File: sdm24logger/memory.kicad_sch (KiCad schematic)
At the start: 5 parts, among them J1 Molex_1040310811, U6 ST_EMIF06-MSD02N16, U7 M24128-BRDW6TP

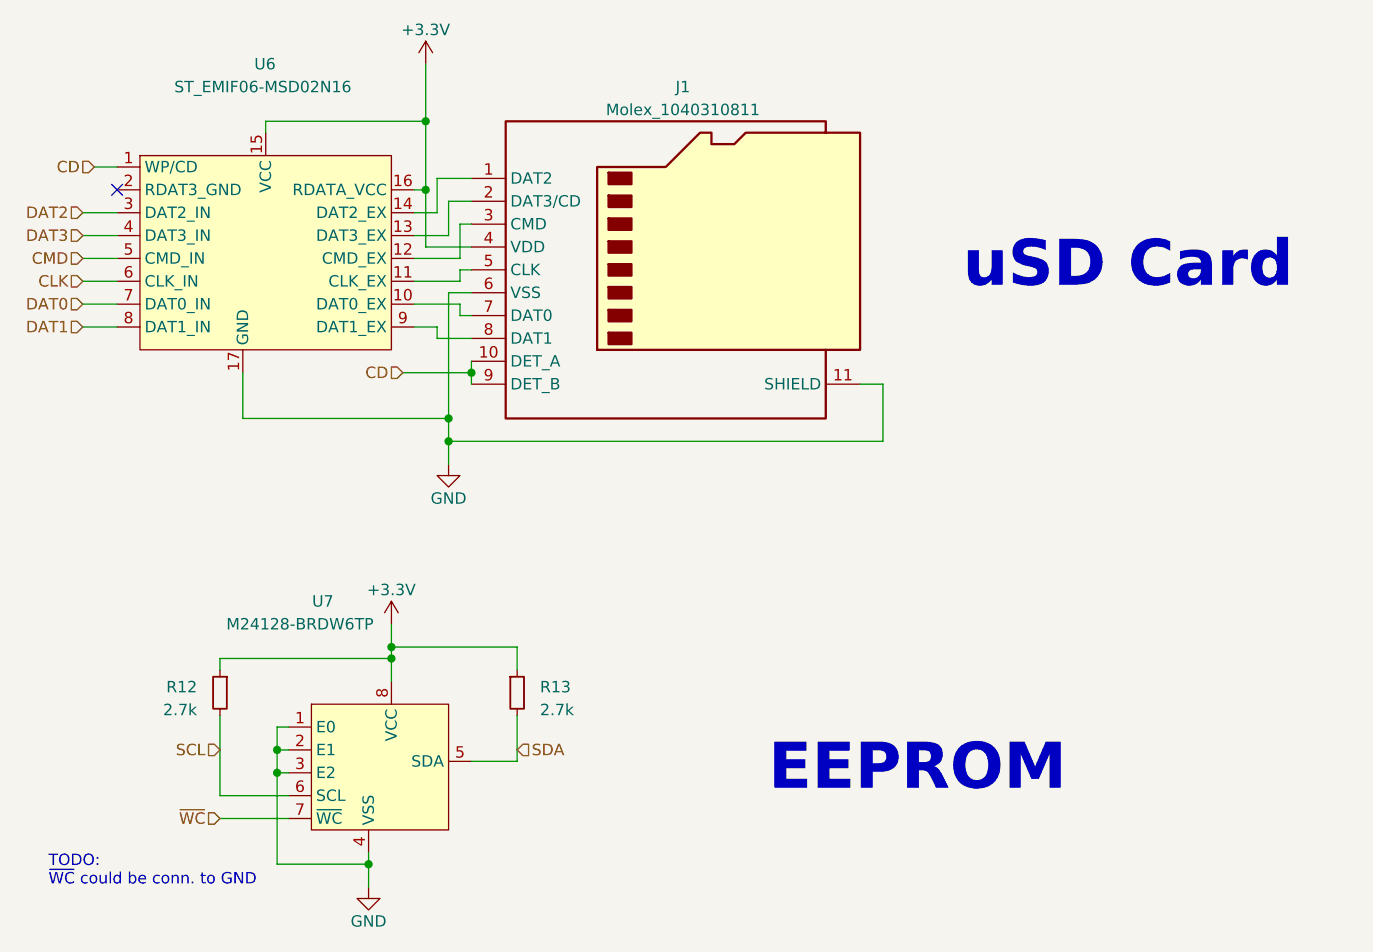
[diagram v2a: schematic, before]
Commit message: add 3d models for data logger
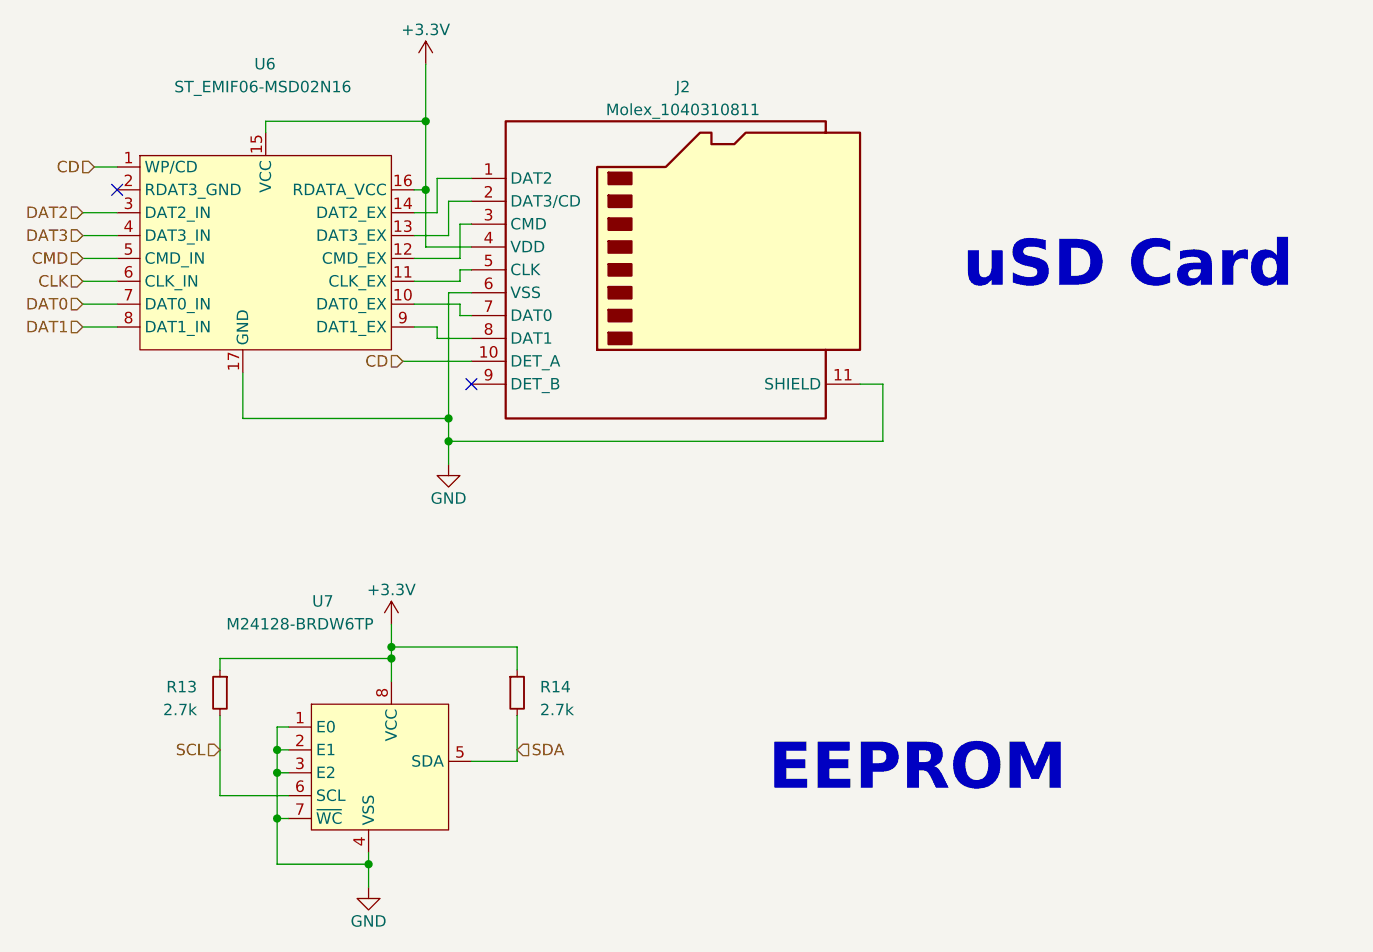
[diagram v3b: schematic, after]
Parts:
- J2: renamed from J1; footprint (none) -> Connector_Card:microSD_HC_Molex_104031-0811
- U7: footprint (none) -> Package_SO:TSSOP-8_4.4x3mm_P0.65mm
- renumbered R12 to R13, R13 to R14
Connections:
- net ~{WC} is gone; now on net GND: U7.7 (~{WC})
- net CD: no longer J2.9 (DET_B)
- no-connect marks 1 -> 2
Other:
- note removed: "TODO: ~{WC} could be conn. to GND"
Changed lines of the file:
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@@
   (title_block
     (title "SDM-24 Data Logger")
-    (date "2023-09-07")
+    (date "2023-10-12")
     (rev "v1")
     (company "Sun Devil Motorsports")
@@
   (junction (at 140.97 86.36) (diameter 0) (color 0 0 0 0)
   )
+  (junction (at 121.92 130.81) (diameter 0) (color 0 0 0 0)
+  )
   (junction (at 121.92 123.19) (diameter 0) (color 0 0 0 0)
   )
-  (junction (at 143.51 81.28) (diameter 0) (color 0 0 0 0)
-  )
+  (no_connect (at 143.51 82.55))
   (no_connect (at 104.14 60.96))
   (wire (pts (xy 189.23 82.55) (xy 189.23 88.9))
@@
     (stroke (width 0) (type default))
   )
-  (wire (pts (xy 115.57 130.81) (xy 123.19 130.81))
-    (stroke (width 0) (type default))
-  )
   (wire (pts (xy 142.24 69.85) (xy 142.24 71.12))
     (stroke (width 0) (type default))
@@
     (stroke (width 0) (type default))
   )
-  (wire (pts (xy 143.51 80.01) (xy 143.51 81.28))
-    (stroke (width 0) (type default))
-  )
   (wire (pts (xy 137.16 76.2) (xy 139.7 76.2))
     (stroke (width 0) (type default))
@@
     (stroke (width 0) (type default))
   )
-  (wire (pts (xy 135.89 81.28) (xy 143.51 81.28))
+  (wire (pts (xy 135.89 80.01) (xy 143.51 80.01))
     (stroke (width 0) (type default))
   )
@@
     (stroke (width 0) (type default))
   )
-  (wire (pts (xy 143.51 81.28) (xy 143.51 82.55))
-    (stroke (width 0) (type default))
-  )
   (wire (pts (xy 115.57 113.03) (xy 134.62 113.03))
     (stroke (width 0) (type default))
@@
     (stroke (width 0) (type default))
   )
+  (wire (pts (xy 121.92 130.81) (xy 121.92 135.89))
+    (stroke (width 0) (type default))
+  )
   (wire (pts (xy 100.33 71.12) (xy 104.14 71.12))
     (stroke (width 0) (type default))
@@
     (stroke (width 0) (type default))
   )
-  (wire (pts (xy 121.92 125.73) (xy 121.92 135.89))
+  (wire (pts (xy 121.92 125.73) (xy 121.92 130.81))
     (stroke (width 0) (type default))
   )
@@
   )
   (wire (pts (xy 189.23 88.9) (xy 140.97 88.9))
+    (stroke (width 0) (type default))
+  )
+  (wire (pts (xy 121.92 130.81) (xy 123.19 130.81))
     (stroke (width 0) (type default))
   )
@@
     (effects (font (size 5.12 5.12) (thickness 1.024) bold) (justify left bottom))
   )
-  (text "TODO: \n~{WC} could be conn. to GND\n" (at 96.52 138.43 0)
-    (effects (font (size 1.27 1.27)) (justify left bottom))
-  )
   (hierarchical_label "CD" (shape input) (at 101.6 58.42 180) (fields_autoplaced)
     (effects (font (size 1.27 1.27)) (justify right))
@@
     (effects (font (size 1.27 1.27)) (justify left))
   )
-  (hierarchical_label "~{WC}" (shape input) (at 115.57 130.81 180) (fields_autoplaced)
-    (effects (font (size 1.27 1.27)) (justify right))
-  )
   (hierarchical_label "DAT0" (shape input) (at 100.33 73.66 180) (fields_autoplaced)
     (effects (font (size 1.27 1.27)) (justify right))
@@
     (effects (font (size 1.27 1.27)) (justify right))
   )
-  (hierarchical_label "CD" (shape input) (at 135.89 81.28 180) (fields_autoplaced)
+  (hierarchical_label "CD" (shape input) (at 135.89 80.01 180) (fields_autoplaced)
     (effects (font (size 1.27 1.27)) (justify right))
   )
   (symbol (lib_id "power:+3.3V") (at 134.62 109.22 0) (unit 1)
     (in_bom yes) (on_board yes) (dnp no) (fields_autoplaced)
-    (property "Reference" "#PWR030" (at 134.62 113.03 0)
+    (property "Reference" "#PWR033" (at 134.62 113.03 0)
       (effects (font (size 1.27 1.27)) hide)
     )
@@
       (project "sdm24logger"
         (path "/89b3ea44-cadd-4bd5-8c60-f45fe49f0b09/755989b5-01b1-4d90-aab7-caeafb9cb82b"
-          (reference "#PWR030") (unit 1)
+          (reference "#PWR033") (unit 1)
         )
       )
@@
   (symbol (lib_id "Device:R_Small") (at 115.57 116.84 0) (mirror y) (unit 1)
     (in_bom yes) (on_board yes) (dnp no)
-    (property "Reference" "R12" (at 113.03 116.205 0)
+    (property "Reference" "R13" (at 113.03 116.205 0)
       (effects (font (size 1.27 1.27)) (justify left))
     )
@@
       (project "sdm24logger"
         (path "/89b3ea44-cadd-4bd5-8c60-f45fe49f0b09/755989b5-01b1-4d90-aab7-caeafb9cb82b"
-          (reference "R12") (unit 1)
+          (reference "R13") (unit 1)
         )
       )
@@
       (effects (font (size 1.27 1.27)))
     )
-    (property "Footprint" "" (at 133.35 110.49 0)
+    (property "Footprint" "Package_SO:TSSOP-8_4.4x3mm_P0.65mm" (at 133.35 110.49 0)
       (effects (font (size 1.27 1.27)) hide)
     )
@@
   (symbol (lib_id "power:GND") (at 140.97 91.44 0) (unit 1)
     (in_bom yes) (on_board yes) (dnp no)
-    (property "Reference" "#PWR032" (at 140.97 97.79 0)
+    (property "Reference" "#PWR035" (at 140.97 97.79 0)
       (effects (font (size 1.27 1.27)) hide)
     )
@@
       (project "sdm24logger"
         (path "/89b3ea44-cadd-4bd5-8c60-f45fe49f0b09/755989b5-01b1-4d90-aab7-caeafb9cb82b"
-          (reference "#PWR032") (unit 1)
+          (reference "#PWR035") (unit 1)
         )
       )
@@
   (symbol (lib_id "power:+3.3V") (at 138.43 46.99 0) (unit 1)
     (in_bom yes) (on_board yes) (dnp no) (fields_autoplaced)
-    (property "Reference" "#PWR031" (at 138.43 50.8 0)
+    (property "Reference" "#PWR034" (at 138.43 50.8 0)
       (effects (font (size 1.27 1.27)) hide)
     )
@@
       (project "sdm24logger"
         (path "/89b3ea44-cadd-4bd5-8c60-f45fe49f0b09/755989b5-01b1-4d90-aab7-caeafb9cb82b"
-          (reference "#PWR031") (unit 1)
+          (reference "#PWR034") (unit 1)
         )
       )
@@
   (symbol (lib_id "Connector:Micro_SD_Card_Det2") (at 166.37 69.85 0) (unit 1)
     (in_bom yes) (on_board yes) (dnp no) (fields_autoplaced)
-    (property "Reference" "J1" (at 167.005 49.53 0)
+    (property "Reference" "J2" (at 167.005 49.53 0)
       (effects (font (size 1.27 1.27)))
     )
@@
       (effects (font (size 1.27 1.27)))
     )
-    (property "Footprint" "" (at 218.44 52.07 0)
+    (property "Footprint" "Connector_Card:microSD_HC_Molex_104031-0811" (at 218.44 52.07 0)
       (effects (font (size 1.27 1.27)) hide)
     )
@@
       (project "sdm24logger"
         (path "/89b3ea44-cadd-4bd5-8c60-f45fe49f0b09/755989b5-01b1-4d90-aab7-caeafb9cb82b"
-          (reference "J1") (unit 1)
+          (reference "J2") (unit 1)
         )
       )
@@
   (symbol (lib_id "Device:R_Small") (at 148.59 116.84 0) (unit 1)
     (in_bom yes) (on_board yes) (dnp no) (fields_autoplaced)
-    (property "Reference" "R13" (at 151.13 116.205 0)
+    (property "Reference" "R14" (at 151.13 116.205 0)
       (effects (font (size 1.27 1.27)) (justify left))
     )
@@
       (project "sdm24logger"
         (path "/89b3ea44-cadd-4bd5-8c60-f45fe49f0b09/755989b5-01b1-4d90-aab7-caeafb9cb82b"
-          (reference "R13") (unit 1)
+          (reference "R14") (unit 1)
         )
       )
@@
   (symbol (lib_id "power:GND") (at 132.08 138.43 0) (unit 1)
     (in_bom yes) (on_board yes) (dnp no)
-    (property "Reference" "#PWR029" (at 132.08 144.78 0)
+    (property "Reference" "#PWR032" (at 132.08 144.78 0)
       (effects (font (size 1.27 1.27)) hide)
     )
@@
       (project "sdm24logger"
         (path "/89b3ea44-cadd-4bd5-8c60-f45fe49f0b09/755989b5-01b1-4d90-aab7-caeafb9cb82b"
-          (reference "#PWR029") (unit 1)
-        )
-      )
+          (reference "#PWR032") (unit 1)
+        )
+      )

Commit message: smps layout, power mux
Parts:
- R13, R14: footprint (none) -> Resistor_SMD:R_0603_1608Metric
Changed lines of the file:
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@@
       (effects (font (size 1.27 1.27)) (justify left))
     )
-    (property "Footprint" "" (at 115.57 116.84 0)
+    (property "Footprint" "Resistor_SMD:R_0603_1608Metric" (at 115.57 116.84 0)
       (effects (font (size 1.27 1.27)) hide)
     )
@@
       (effects (font (size 1.27 1.27)) (justify left))
     )
-    (property "Footprint" "" (at 148.59 116.84 0)
+    (property "Footprint" "Resistor_SMD:R_0603_1608Metric" (at 148.59 116.84 0)
       (effects (font (size 1.27 1.27)) hide)
     )

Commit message: planning for external adc
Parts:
- added C33: 100nF, Capacitor_SMD:C_0402_1005Metric, symbol Device:C_Small
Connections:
- net +3.3V: now also C33.1
- net GND: now also C33.2
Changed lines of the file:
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@@
   (junction (at 140.97 86.36) (diameter 0) (color 0 0 0 0)
+  )
+  (junction (at 134.62 110.49) (diameter 0) (color 0 0 0 0)
   )
   (junction (at 121.92 130.81) (diameter 0) (color 0 0 0 0)
@@
     (stroke (width 0) (type default))
   )
+  (wire (pts (xy 134.62 110.49) (xy 160.02 110.49))
+    (stroke (width 0) (type default))
+  )
   (wire (pts (xy 137.16 66.04) (xy 140.97 66.04))
     (stroke (width 0) (type default))
@@
     (stroke (width 0) (type default))
   )
-  (wire (pts (xy 134.62 109.22) (xy 134.62 111.76))
+  (wire (pts (xy 134.62 110.49) (xy 134.62 111.76))
+    (stroke (width 0) (type default))
+  )
+  (wire (pts (xy 134.62 109.22) (xy 134.62 110.49))
     (stroke (width 0) (type default))
   )
@@
     (stroke (width 0) (type default))
   )
+  (wire (pts (xy 160.02 116.84) (xy 160.02 118.11))
+    (stroke (width 0) (type default))
+  )
   (wire (pts (xy 142.24 74.93) (xy 143.51 74.93))
+    (stroke (width 0) (type default))
+  )
+  (wire (pts (xy 160.02 110.49) (xy 160.02 111.76))
     (stroke (width 0) (type default))
   )
@@
     )
   )
+  (symbol (lib_id "Device:C_Small") (at 160.02 114.3 0) (unit 1)
+    (in_bom yes) (on_board yes) (dnp no) (fields_autoplaced)
+    (property "Reference" "C33" (at 162.56 113.6713 0)
+      (effects (font (size 1.27 1.27)) (justify left))
+    )
+    (property "Value" "100nF" (at 162.56 116.2113 0)
+      (effects (font (size 1.27 1.27)) (justify left))
+    )
+    (property "Footprint" "Capacitor_SMD:C_0402_1005Metric" (at 160.02 114.3 0)
+      (effects (font (size 1.27 1.27)) hide)
+    )
+    (property "Datasheet" "~" (at 160.02 114.3 0)
+      (effects (font (size 1.27 1.27)) hide)
+    )
+    (pin "1")
+    (pin "2")
+    (instances
+      (project "sdm24logger"
+        (path "/89b3ea44-cadd-4bd5-8c60-f45fe49f0b09/755989b5-01b1-4d90-aab7-caeafb9cb82b"
+          (reference "C33") (unit 1)
+        )
+      )
+    )
+  )
   (symbol (lib_id "power:GND") (at 140.97 91.44 0) (unit 1)
     (in_bom yes) (on_board yes) (dnp no)
@@
         )
       )
+    )
+  )
+  (symbol (lib_id "power:GND") (at 160.02 118.11 0) (unit 1)
+    (in_bom yes) (on_board yes) (dnp no)
+    (property "Reference" "#PWR059" (at 160.02 124.46 0)
+      (effects (font (size 1.27 1.27)) hide)
+    )
+    (property "Value" "GND" (at 160.02 121.92 0)
+      (effects (font (size 1.27 1.27)))
+    )
+    (property "Footprint" "" (at 160.02 118.11 0)
+      (effects (font (size 1.27 1.27)) hide)
+    )
+    (property "Datasheet" "" (at 160.02 118.11 0)
+      (effects (font (size 1.27 1.27)) hide)
+    )
+    (pin "1")
+    (instances
+      (project "sdm24logger"
+        (path "/89b3ea44-cadd-4bd5-8c60-f45fe49f0b09/755989b5-01b1-4d90-aab7-caeafb9cb82b"
+          (reference "#PWR059") (unit 1)
+        )
+      )

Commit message: ADC pinouts
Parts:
- removed R13, R14: 2.7k, Resistor_SMD:R_0603_1608Metric, symbol Device:R_Small
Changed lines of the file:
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@@
   (title_block
     (title "SDM-24 Data Logger")
-    (date "2023-10-12")
+    (date "2023-10-22")
     (rev "v1")
     (company "Sun Devil Motorsports")
@@
         (path "/89b3ea44-cadd-4bd5-8c60-f45fe49f0b09/755989b5-01b1-4d90-aab7-caeafb9cb82b"
           (reference "#PWR033") (unit 1)
-        )
-      )
-    )
-  )
-  (symbol (lib_id "Device:R_Small") (at 115.57 116.84 0) (mirror y) (unit 1)
-    (in_bom yes) (on_board yes) (dnp no)
-    (property "Reference" "R13" (at 113.03 116.205 0)
-      (effects (font (size 1.27 1.27)) (justify left))
-    )
-    (property "Value" "2.7k" (at 113.03 118.745 0)
-      (effects (font (size 1.27 1.27)) (justify left))
-    )
-    (property "Footprint" "Resistor_SMD:R_0603_1608Metric" (at 115.57 116.84 0)
-      (effects (font (size 1.27 1.27)) hide)
-    )
-    (property "Datasheet" "~" (at 115.57 116.84 0)
-      (effects (font (size 1.27 1.27)) hide)
-    )
-    (pin "1")
-    (pin "2")
-    (instances
-      (project "sdm24logger"
-        (path "/89b3ea44-cadd-4bd5-8c60-f45fe49f0b09/755989b5-01b1-4d90-aab7-caeafb9cb82b"
-          (reference "R13") (unit 1)
         )
       )
@@
         )
       )
-    )
-  )
-  (symbol (lib_id "Device:R_Small") (at 148.59 116.84 0) (unit 1)
-    (in_bom yes) (on_board yes) (dnp no) (fields_autoplaced)
-    (property "Reference" "R14" (at 151.13 116.205 0)
-      (effects (font (size 1.27 1.27)) (justify left))
-    )
-    (property "Value" "2.7k" (at 151.13 118.745 0)
-      (effects (font (size 1.27 1.27)) (justify left))
-    )
-    (property "Footprint" "Resistor_SMD:R_0603_1608Metric" (at 148.59 116.84 0)
-      (effects (font (size 1.27 1.27)) hide)
-    )
-    (property "Datasheet" "~" (at 148.59 116.84 0)
-      (effects (font (size 1.27 1.27)) hide)
-    )
-    (pin "1")
-    (pin "2")
-    (instances
-      (project "sdm24logger"
-        (path "/89b3ea44-cadd-4bd5-8c60-f45fe49f0b09/755989b5-01b1-4d90-aab7-caeafb9cb82b"
-          (reference "R14") (unit 1)
-        )
-      )

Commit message: uploading changes
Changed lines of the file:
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@@
     (comment 1 "SD card and EEPROM circuitry")
   )
-  (junction (at 134.62 113.03) (diameter 0) (color 0 0 0 0)
-  )
   (junction (at 140.97 88.9) (diameter 0) (color 0 0 0 0)
-  )
-  (junction (at 134.62 111.76) (diameter 0) (color 0 0 0 0)
   )
   (junction (at 132.08 135.89) (diameter 0) (color 0 0 0 0)
@@
     (stroke (width 0) (type default))
   )
-  (wire (pts (xy 134.62 111.76) (xy 134.62 113.03))
+  (wire (pts (xy 134.62 110.49) (xy 134.62 115.57))
     (stroke (width 0) (type default))
   )
@@
     (stroke (width 0) (type default))
   )
-  (wire (pts (xy 115.57 119.38) (xy 115.57 128.27))
-    (stroke (width 0) (type default))
-  )
   (wire (pts (xy 123.19 120.65) (xy 121.92 120.65))
     (stroke (width 0) (type default))
   )
-  (wire (pts (xy 115.57 114.3) (xy 115.57 113.03))
-    (stroke (width 0) (type default))
-  )
   (wire (pts (xy 123.19 125.73) (xy 121.92 125.73))
     (stroke (width 0) (type default))
@@
     (stroke (width 0) (type default))
   )
+  (wire (pts (xy 119.38 128.27) (xy 123.19 128.27))
+    (stroke (width 0) (type default))
+  )
   (wire (pts (xy 137.16 66.04) (xy 140.97 66.04))
     (stroke (width 0) (type default))
@@
     (stroke (width 0) (type default))
   )
-  (wire (pts (xy 134.62 113.03) (xy 134.62 115.57))
-    (stroke (width 0) (type default))
-  )
   (wire (pts (xy 138.43 60.96) (xy 138.43 53.34))
     (stroke (width 0) (type default))
@@
     (stroke (width 0) (type default))
   )
-  (wire (pts (xy 134.62 110.49) (xy 134.62 111.76))
-    (stroke (width 0) (type default))
-  )
   (wire (pts (xy 134.62 109.22) (xy 134.62 110.49))
     (stroke (width 0) (type default))
   )
-  (wire (pts (xy 148.59 124.46) (xy 143.51 124.46))
-    (stroke (width 0) (type default))
-  )
   (wire (pts (xy 100.33 68.58) (xy 104.14 68.58))
     (stroke (width 0) (type default))
@@
     (stroke (width 0) (type default))
   )
-  (wire (pts (xy 148.59 114.3) (xy 148.59 111.76))
-    (stroke (width 0) (type default))
-  )
   (wire (pts (xy 142.24 73.66) (xy 142.24 74.93))
     (stroke (width 0) (type default))
@@
     (stroke (width 0) (type default))
   )
-  (wire (pts (xy 148.59 119.38) (xy 148.59 124.46))
+  (wire (pts (xy 143.51 124.46) (xy 146.05 124.46))
     (stroke (width 0) (type default))
   )
@@
     (stroke (width 0) (type default))
   )
-  (wire (pts (xy 115.57 128.27) (xy 123.19 128.27))
-    (stroke (width 0) (type default))
-  )
   (wire (pts (xy 137.16 68.58) (xy 142.24 68.58))
     (stroke (width 0) (type default))
@@
     (stroke (width 0) (type default))
   )
-  (wire (pts (xy 115.57 113.03) (xy 134.62 113.03))
-    (stroke (width 0) (type default))
-  )
   (wire (pts (xy 139.7 59.69) (xy 139.7 63.5))
     (stroke (width 0) (type default))
@@
   )
   (wire (pts (xy 121.92 135.89) (xy 132.08 135.89))
-    (stroke (width 0) (type default))
-  )
-  (wire (pts (xy 148.59 111.76) (xy 134.62 111.76))
     (stroke (width 0) (type default))
   )
@@
     (effects (font (size 1.27 1.27)) (justify right))
   )
-  (hierarchical_label "SDA" (shape input) (at 148.59 123.19 0) (fields_autoplaced)
+  (hierarchical_label "SDA" (shape input) (at 146.05 124.46 0) (fields_autoplaced)
     (effects (font (size 1.27 1.27)) (justify left))
   )
@@
     (effects (font (size 1.27 1.27)) (justify right))
   )
-  (hierarchical_label "SCL" (shape input) (at 115.57 123.19 180) (fields_autoplaced)
-    (effects (font (size 1.27 1.27)) (justify right))
-  )
+  (hierarchical_label "SCL" (shape input) (at 119.38 128.27 180) (fields_autoplaced)
+    (effects (font (size 1.27 1.27)) (justify right))
+  )
